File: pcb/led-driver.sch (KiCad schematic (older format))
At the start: 17 parts, among them P201 CONN_01X01, P202 CONN_01X01, P203 CONN_01X01, P204 CONN_01X01, Q201 Q_NMOS_GDSD, Q202 Q_NMOS_GDSD, Q203 Q_NMOS_GDSD, Q204 Q_NMOS_GDSD, U201 LM2902N, U202 MAX5813

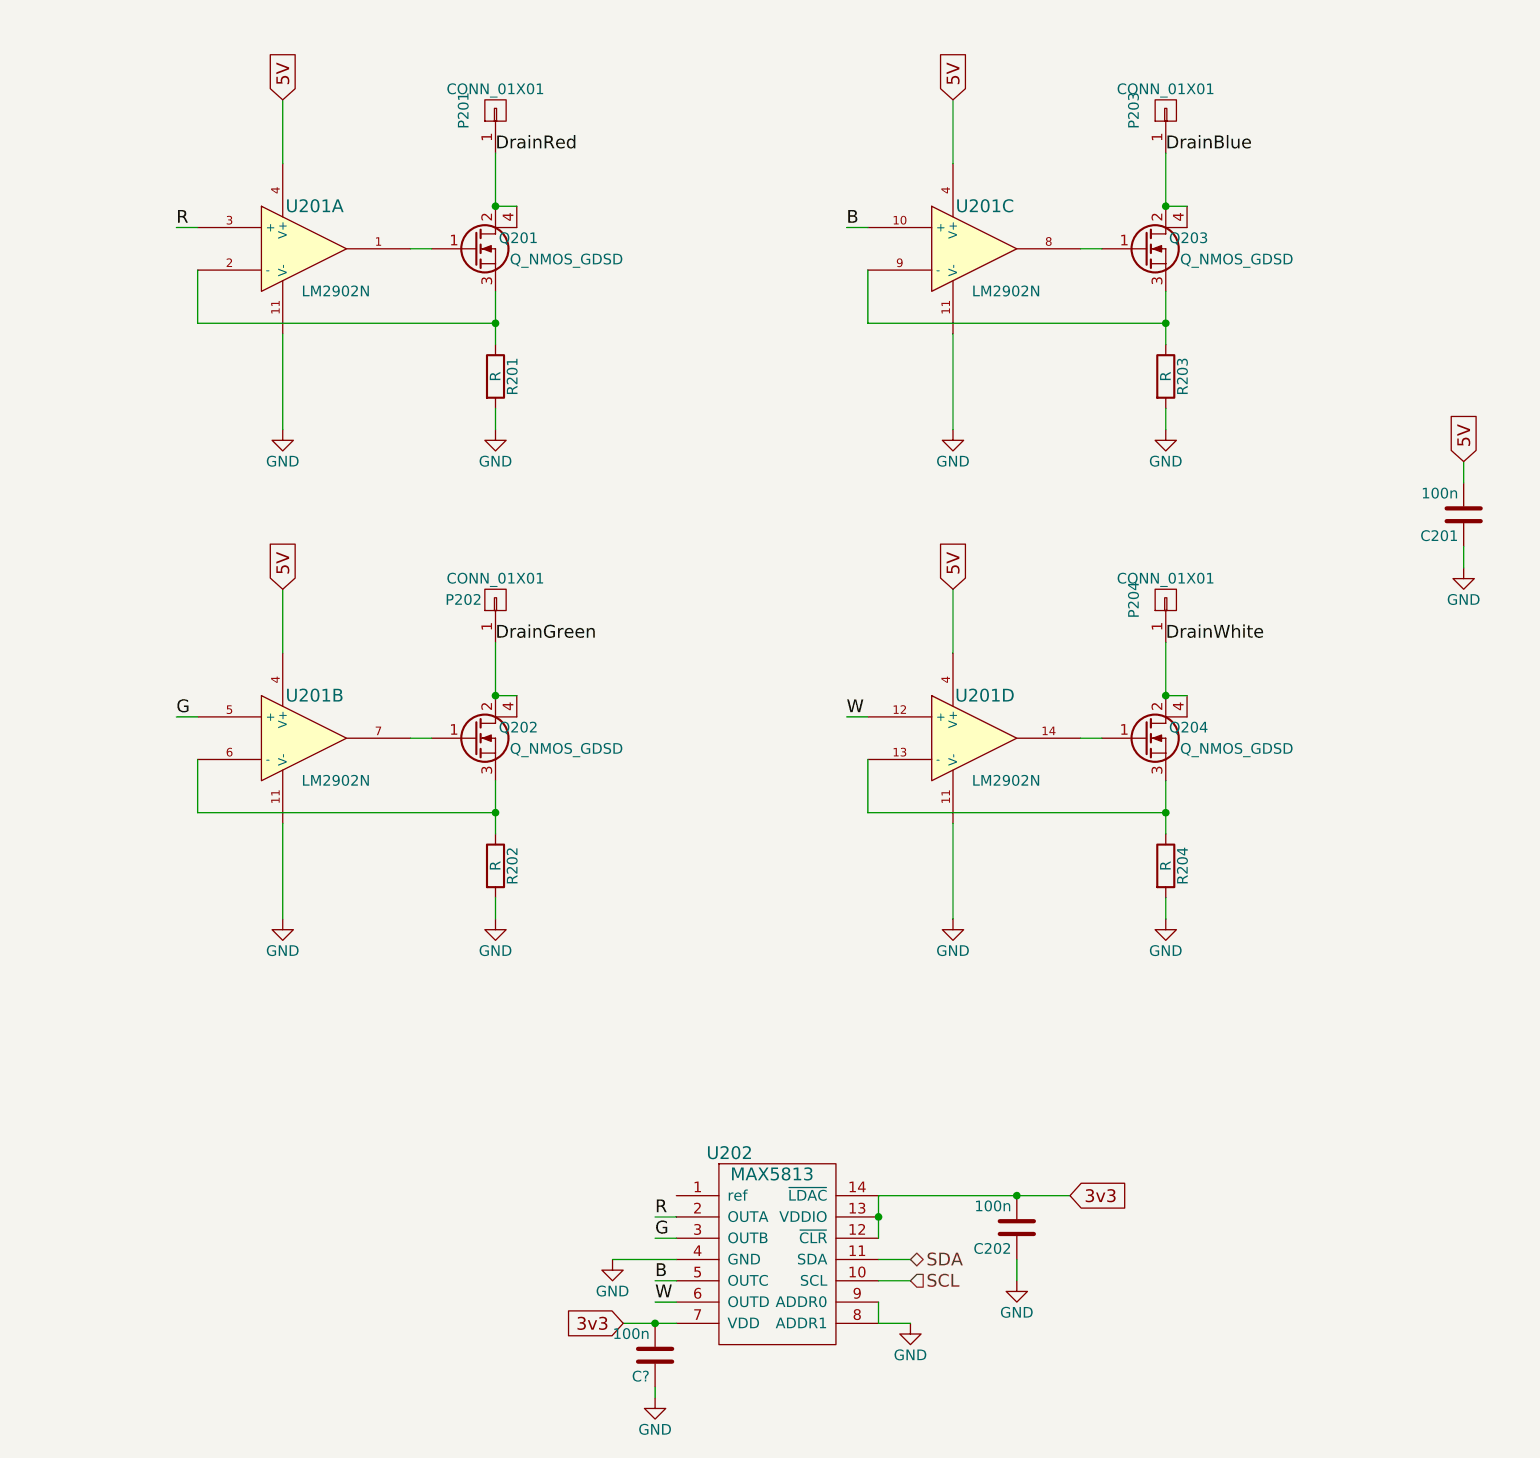
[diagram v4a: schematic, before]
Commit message: started work on 2 layered version
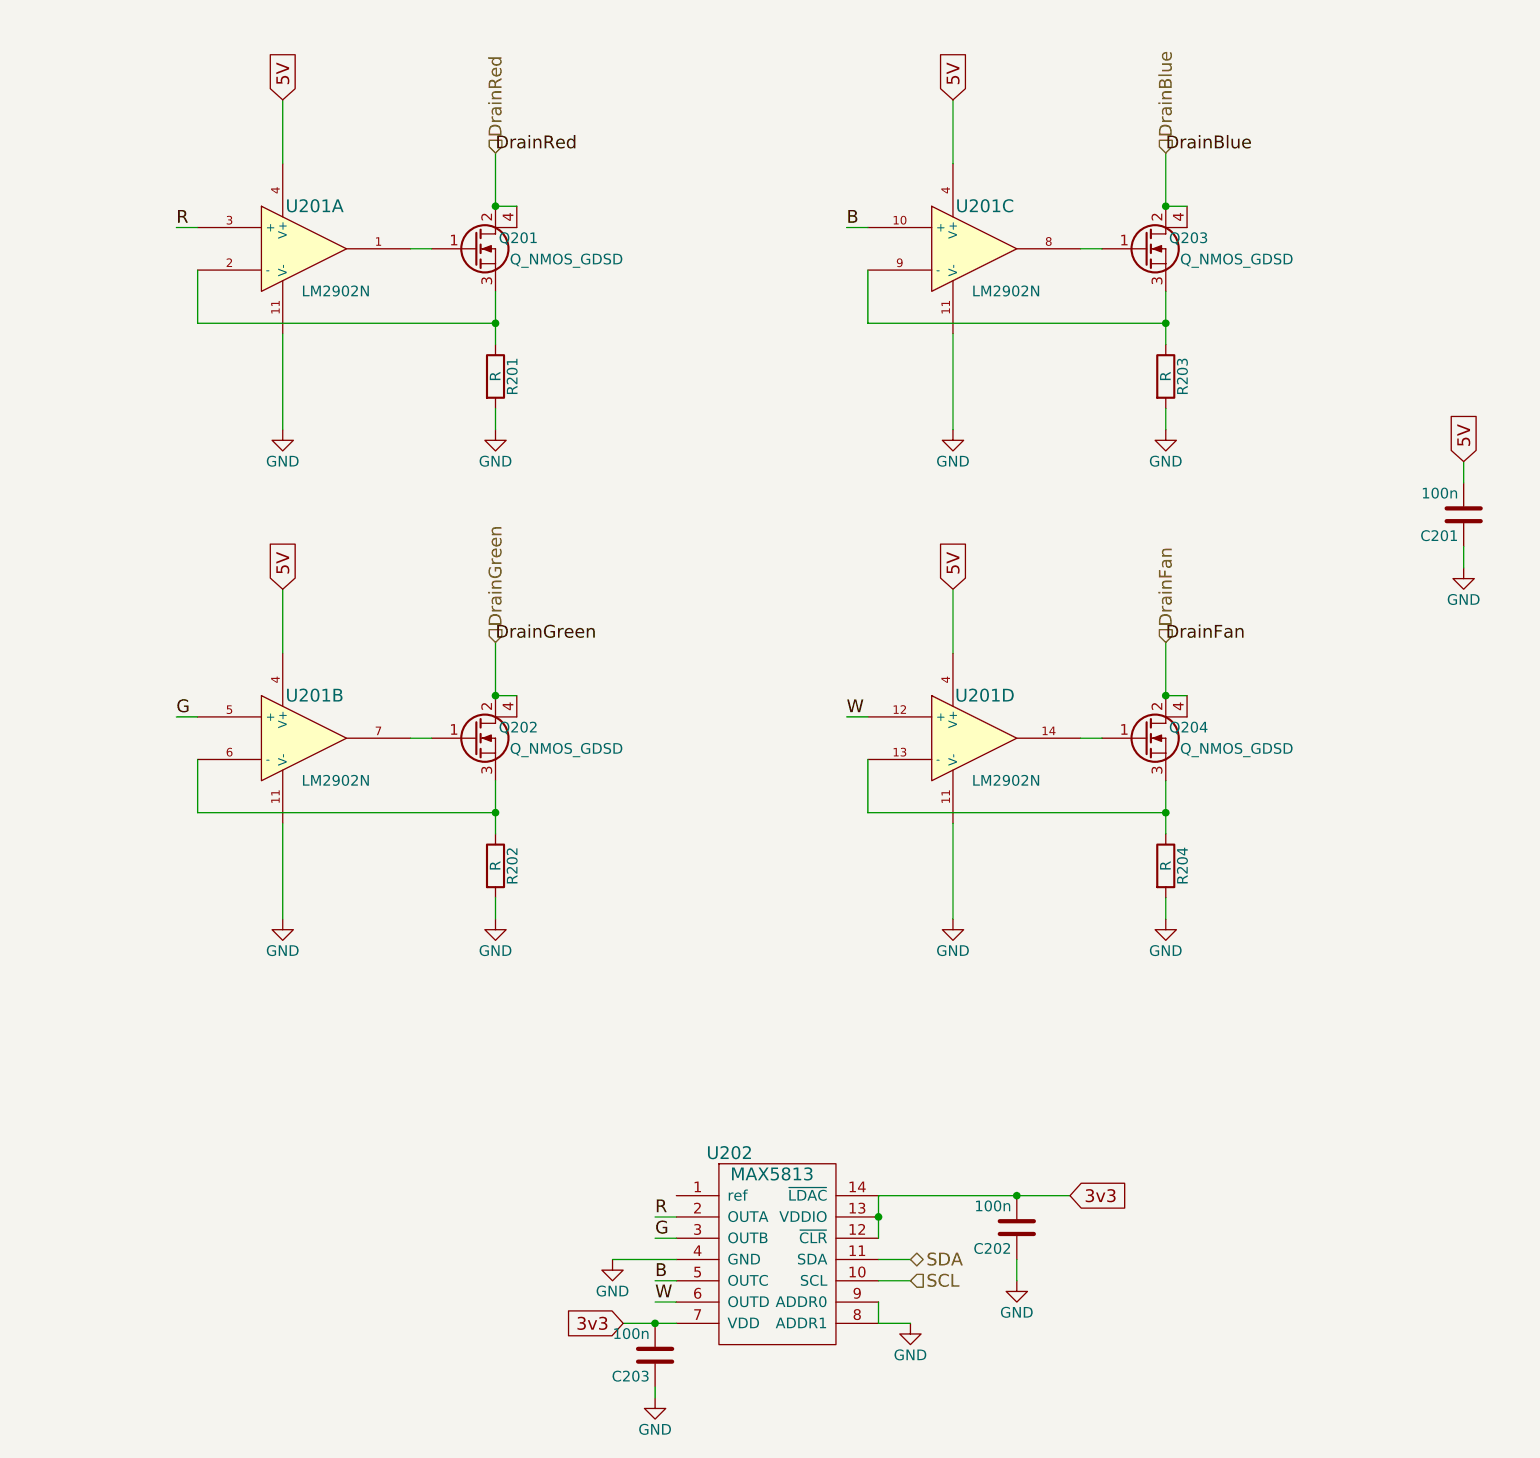
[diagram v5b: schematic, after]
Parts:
- removed P201, P202, P203, P204: CONN_01X01, netl:1Pin_big, symbol CONN_01X01
- gave numbers to parts that had none: 1
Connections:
- net DrainWhite renamed DrainFan
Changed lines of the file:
@@
 $EndDescr
 $Comp
-L GND #PWR08
+L GND #PWR09
 U 1 1 566DBED0
 P 3200 2550
-F 0 "#PWR08" H 3200 2300 50  0001 C CNN
+F 0 "#PWR09" H 3200 2300 50  0001 C CNN
 F 1 "GND" H 3200 2400 50  0000 C CNN
 F 2 "" H 3200 2550 60  0000 C CNN
@@
 	1    3200 2550
 	1    0    0    -1
-$EndComp
-$Comp
-L CONN_01X01 P201
-U 1 1 566DBF4F
-P 3200 1050
-F 0 "P201" H 3200 1200 50  0000 C CNN
-F 1 "CONN_01X01" V 3300 1050 50  0000 C CNN
-F 2 "netl:1Pin_big" H 3200 1050 60  0001 C CNN
-F 3 "" H 3200 1050 60  0000 C CNN
-	1    3200 1050
-	0    -1   -1   0
 $EndComp
 Text Label 6350 1250 0    60   ~ 0
@@
 	1800 2050 1800 1800
 $Comp
-L GND #PWR09
+L GND #PWR010
 U 1 1 566DE548
 P 2200 2550
-F 0 "#PWR09" H 2200 2300 50  0001 C CNN
+F 0 "#PWR010" H 2200 2300 50  0001 C CNN
 F 1 "GND" H 2200 2400 50  0000 C CNN
 F 2 "" H 2200 2550 60  0000 C CNN
@@
 	3200 1250 3200 1500
 $Comp
-L GND #PWR010
+L GND #PWR011
 U 1 1 566E450E
 P 3200 4850
-F 0 "#PWR010" H 3200 4600 50  0001 C CNN
+F 0 "#PWR011" H 3200 4600 50  0001 C CNN
 F 1 "GND" H 3200 4700 50  0000 C CNN
 F 2 "" H 3200 4850 60  0000 C CNN
@@
 	1    3200 4850
 	1    0    0    -1
-$EndComp
-$Comp
-L CONN_01X01 P202
-U 1 1 566E4519
-P 3200 3350
-F 0 "P202" V 3200 3500 50  0000 C CNN
-F 1 "CONN_01X01" V 3300 3350 50  0000 C CNN
-F 2 "netl:1Pin_big" H 3200 3350 60  0001 C CNN
-F 3 "" H 3200 3350 60  0000 C CNN
-	1    3200 3350
-	0    -1   -1   0
 $EndComp
 $Comp
@@
 	1800 4350 1800 4100
 $Comp
-L GND #PWR011
+L GND #PWR012
 U 1 1 566E453D
 P 2200 4850
-F 0 "#PWR011" H 2200 4600 50  0001 C CNN
+F 0 "#PWR012" H 2200 4600 50  0001 C CNN
 F 1 "GND" H 2200 4700 50  0000 C CNN
 F 2 "" H 2200 4850 60  0000 C CNN
@@
 	3200 3550 3200 3800
 $Comp
-L GND #PWR012
+L GND #PWR013
 U 1 1 566E478C
 P 6350 2550
-F 0 "#PWR012" H 6350 2300 50  0001 C CNN
+F 0 "#PWR013" H 6350 2300 50  0001 C CNN
 F 1 "GND" H 6350 2400 50  0000 C CNN
 F 2 "" H 6350 2550 60  0000 C CNN
@@
 	1    6350 2550
 	1    0    0    -1
-$EndComp
-$Comp
-L CONN_01X01 P203
-U 1 1 566E4797
-P 6350 1050
-F 0 "P203" H 6350 1200 50  0000 C CNN
-F 1 "CONN_01X01" V 6450 1050 50  0000 C CNN
-F 2 "netl:1Pin_big" H 6350 1050 60  0001 C CNN
-F 3 "" H 6350 1050 60  0000 C CNN
-	1    6350 1050
-	0    -1   -1   0
 $EndComp
 $Comp
@@
 	4950 2050 4950 1800
 $Comp
-L GND #PWR013
+L GND #PWR014
 U 1 1 566E47BB
 P 5350 2550
-F 0 "#PWR013" H 5350 2300 50  0001 C CNN
+F 0 "#PWR014" H 5350 2300 50  0001 C CNN
 F 1 "GND" H 5350 2400 50  0000 C CNN
 F 2 "" H 5350 2550 60  0000 C CNN
@@
 $EndComp
 $Comp
-L GND #PWR014
+L GND #PWR015
 U 1 1 566E84F5
 P 3750 6450
-F 0 "#PWR014" H 3750 6200 50  0001 C CNN
+F 0 "#PWR015" H 3750 6200 50  0001 C CNN
 F 1 "GND" H 3750 6300 50  0000 C CNN
 F 2 "" H 3750 6450 60  0000 C CNN
@@
 	5000 6550 5150 6550
 $Comp
-L GND #PWR015
+L GND #PWR016
 U 1 1 566E8506
 P 5150 6750
-F 0 "#PWR015" H 5150 6500 50  0001 C CNN
+F 0 "#PWR016" H 5150 6500 50  0001 C CNN
 F 1 "GND" H 5150 6600 50  0000 C CNN
 F 2 "" H 5150 6750 60  0000 C CNN
@@
 	1700 1600 1800 1600
 Text Label 6350 3550 0    60   ~ 0
-DrainWhite
-$Comp
-L GND #PWR016
+DrainFan
+$Comp
+L GND #PWR017
 U 1 1 566E01A5
 P 6350 4850
-F 0 "#PWR016" H 6350 4600 50  0001 C CNN
+F 0 "#PWR017" H 6350 4600 50  0001 C CNN
 F 1 "GND" H 6350 4700 50  0000 C CNN
 F 2 "" H 6350 4850 60  0000 C CNN
@@
 	1    6350 4850
 	1    0    0    -1
-$EndComp
-$Comp
-L CONN_01X01 P204
-U 1 1 566E01AE
-P 6350 3350
-F 0 "P204" H 6350 3500 50  0000 C CNN
-F 1 "CONN_01X01" V 6450 3350 50  0000 C CNN
-F 2 "netl:1Pin_big" H 6350 3350 60  0001 C CNN
-F 3 "" H 6350 3350 60  0000 C CNN
-	1    6350 3350
-	0    -1   -1   0
 $EndComp
 $Comp
@@
 	4950 4350 4950 4100
 $Comp
-L GND #PWR017
+L GND #PWR018
 U 1 1 566E01CE
 P 5350 4850
-F 0 "#PWR017" H 5350 4600 50  0001 C CNN
+F 0 "#PWR018" H 5350 4600 50  0001 C CNN
 F 1 "GND" H 5350 4700 50  0000 C CNN
 F 2 "" H 5350 4850 60  0000 C CNN
@@
 5V
 $Comp
-L GND #PWR018
+L GND #PWR019
 U 1 1 566EAF9B
 P 7750 3200
-F 0 "#PWR018" H 7750 2950 50  0001 C CNN
+F 0 "#PWR019" H 7750 2950 50  0001 C CNN
 F 1 "GND" H 7750 3050 50  0000 C CNN
 F 2 "" H 7750 3200 60  0000 C CNN
@@
 $EndComp
 $Comp
-L GND #PWR019
+L GND #PWR020
 U 1 1 56B92263
 P 5650 6550
-F 0 "#PWR019" H 5650 6300 50  0001 C CNN
+F 0 "#PWR020" H 5650 6300 50  0001 C CNN
 F 1 "GND" H 5650 6400 50  0000 C CNN
 F 2 "" H 5650 6550 60  0000 C CNN
@@
 Connection ~ 5650 6150
 $Comp
-L C C?
+L C C203
 U 1 1 56B92AE4
 P 3950 6900
-F 0 "C?" H 3975 7000 50  0000 L CNN
+F 0 "C203" H 3975 7000 50  0000 L CNN
 F 1 "100n" H 3975 6800 50  0000 L CNN
 F 2 "netl:SMD_0603" H 3988 6750 30  0001 C CNN
@@
 Connection ~ 3950 6750
 $Comp
-L GND #PWR?
+L GND #PWR021
 U 1 1 56B92D0C
 P 3950 7100
-F 0 "#PWR?" H 3950 6850 50  0001 C CNN
+F 0 "#PWR021" H 3950 6850 50  0001 C CNN
 F 1 "GND" H 3950 6950 50  0000 C CNN
 F 2 "" H 3950 7100 60  0000 C CNN
@@
 Wire Wire Line
 	3950 7050 3950 7100
+Text HLabel 3200 1250 1    60   Input ~ 0
+DrainRed
+Text HLabel 3200 3550 1    60   Input ~ 0
+DrainGreen
+Text HLabel 6350 1250 1    60   Input ~ 0
+DrainBlue
+Text HLabel 6350 3550 1    60   Input ~ 0
+DrainFan
 $EndSCHEMATC
